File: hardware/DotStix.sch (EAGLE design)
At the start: 15 parts, among them U1 ATMEGA328P-MU-QFN32

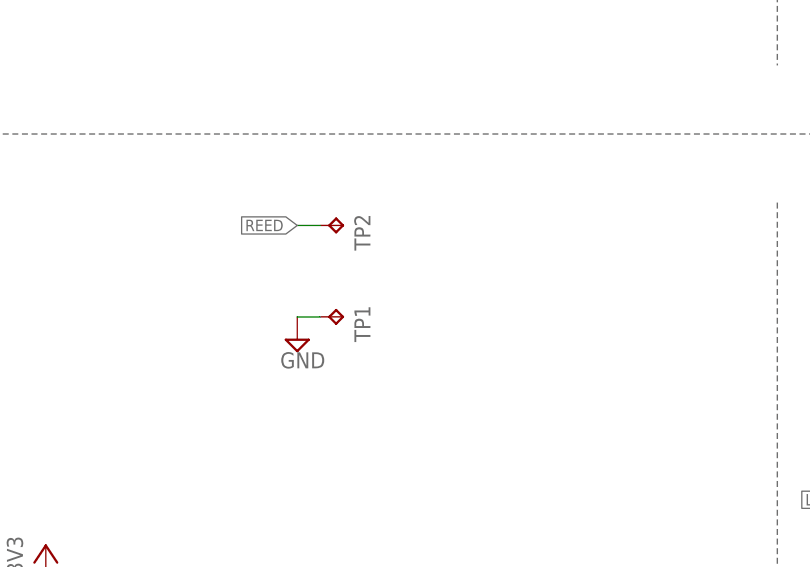
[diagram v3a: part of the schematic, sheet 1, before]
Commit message: Add HexID, second reed on rear side
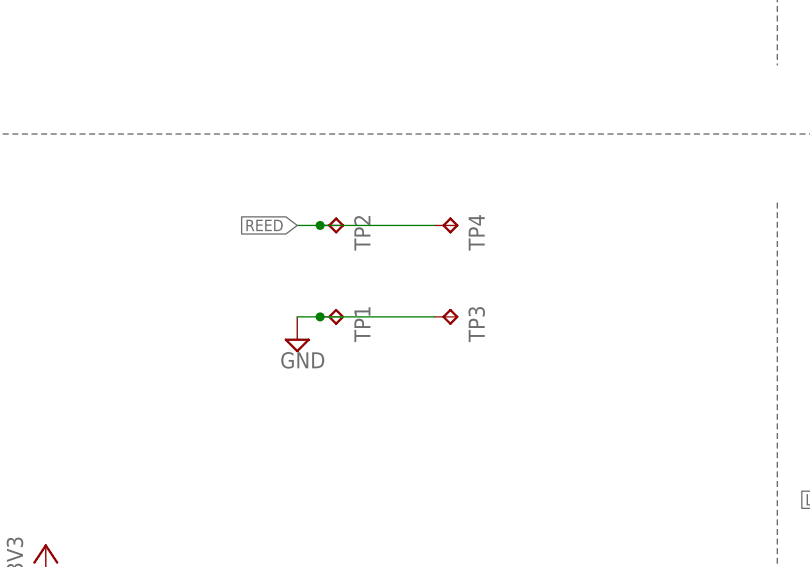
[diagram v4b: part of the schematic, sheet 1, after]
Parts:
- added TP3, TP4: TPTP20SQ, testpad:TPTP20SQ
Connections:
- net GND: now also TP3.TP
- net REED: now also TP4.TP
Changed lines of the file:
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@@
 <part name="+3V9" library="supply1" deviceset="+3V3" device=""/>
 <part name="SUPPLY10" library="supply2" deviceset="GND" device=""/>
+<part name="TP3" library="testpad" deviceset="TP" device="TP20SQ"/>
+<part name="TP4" library="testpad" deviceset="TP" device="TP20SQ"/>
 </parts>
 <sheets>
@@
 <instance part="+3V9" gate="G$1" x="48.26" y="55.88"/>
 <instance part="SUPPLY10" gate="GND" x="-6.35" y="39.37"/>
+<instance part="TP3" gate="G$1" x="93.98" y="81.28" rot="R270"/>
+<instance part="TP4" gate="G$1" x="93.98" y="91.44" rot="R270"/>
 </instances>
 <busses>
@@
 <pinref part="SUPPLY5" gate="GND" pin="GND"/>
 <wire x1="78.74" y1="81.28" x2="76.2" y2="81.28" width="0.1524" layer="91"/>
+<pinref part="TP3" gate="G$1" pin="TP"/>
+<wire x1="91.44" y1="81.28" x2="78.74" y2="81.28" width="0.1524" layer="91"/>
+<junction x="78.74" y="81.28"/>
 </segment>
 <segment>
@@
 <net name="REED" class="0">
 <segment>
+<pinref part="U1" gate="G$1" pin="PB2(SS/OC1B/PCINT2)"/>
+<wire x1="195.58" y1="81.28" x2="198.12" y2="81.28" width="0.1524" layer="91"/>
+<label x="198.12" y="81.28" size="1.27" layer="95" xref="yes"/>
+</segment>
+<segment>
+<pinref part="TP4" gate="G$1" pin="TP"/>
 <pinref part="TP2" gate="G$1" pin="TP"/>
 <wire x1="78.74" y1="91.44" x2="76.2" y2="91.44" width="0.1524" layer="91"/>
 <label x="76.2" y="91.44" size="1.27" layer="95" rot="R180" xref="yes"/>
-</segment>
-<segment>
-<pinref part="U1" gate="G$1" pin="PB2(SS/OC1B/PCINT2)"/>
-<wire x1="195.58" y1="81.28" x2="198.12" y2="81.28" width="0.1524" layer="91"/>
-<label x="198.12" y="81.28" size="1.27" layer="95" xref="yes"/>
-</segment>
-</net>
+<wire x1="91.44" y1="91.44" x2="78.74" y2="91.44" width="0.1524" layer="91"/>
+<junction x="78.74" y="91.44"/>
+</segment>
+</net>

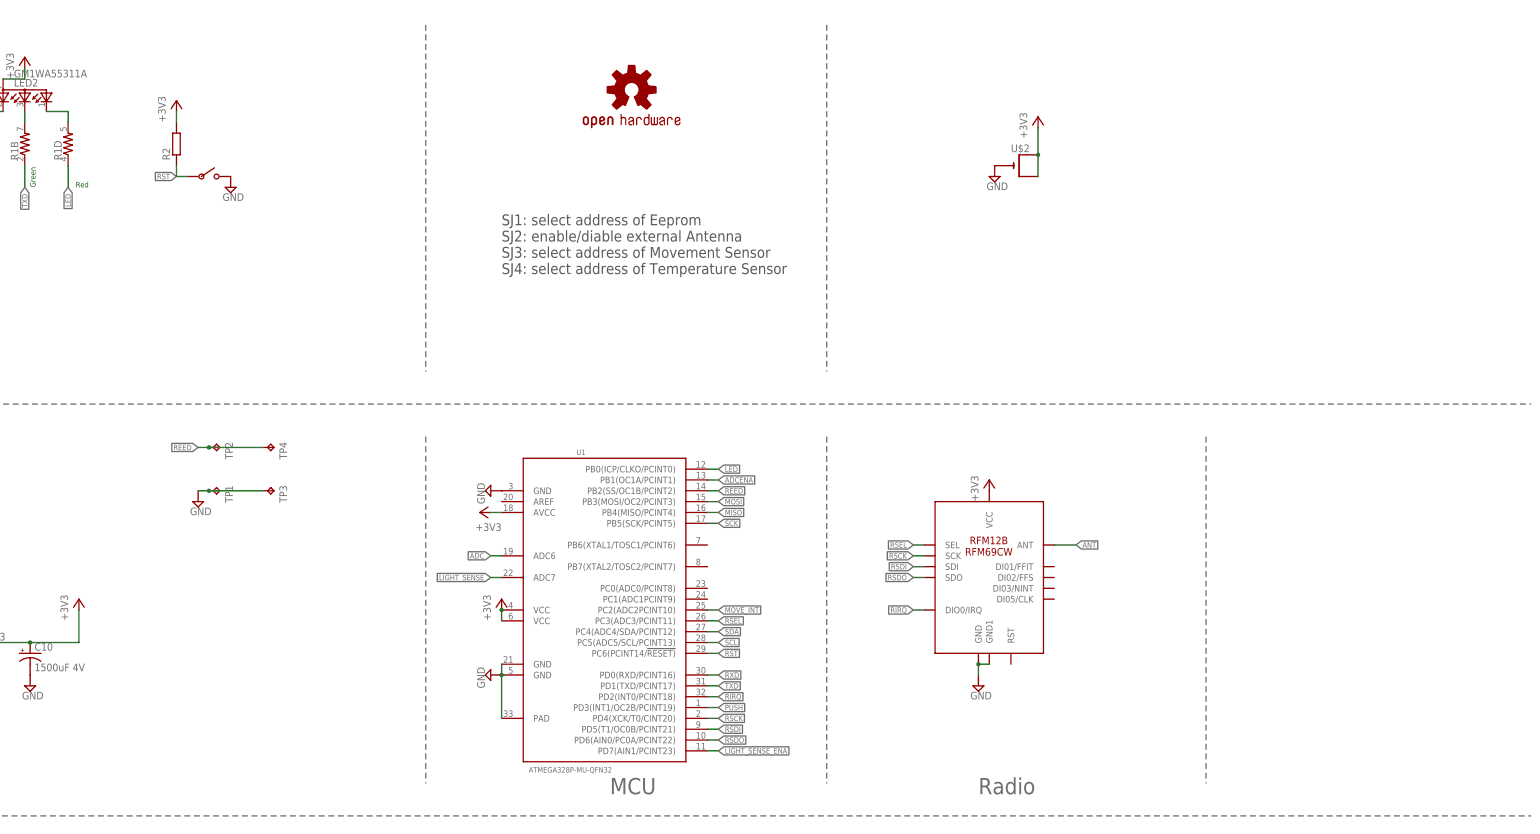
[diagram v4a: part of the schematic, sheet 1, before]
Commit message: Add photoresistor
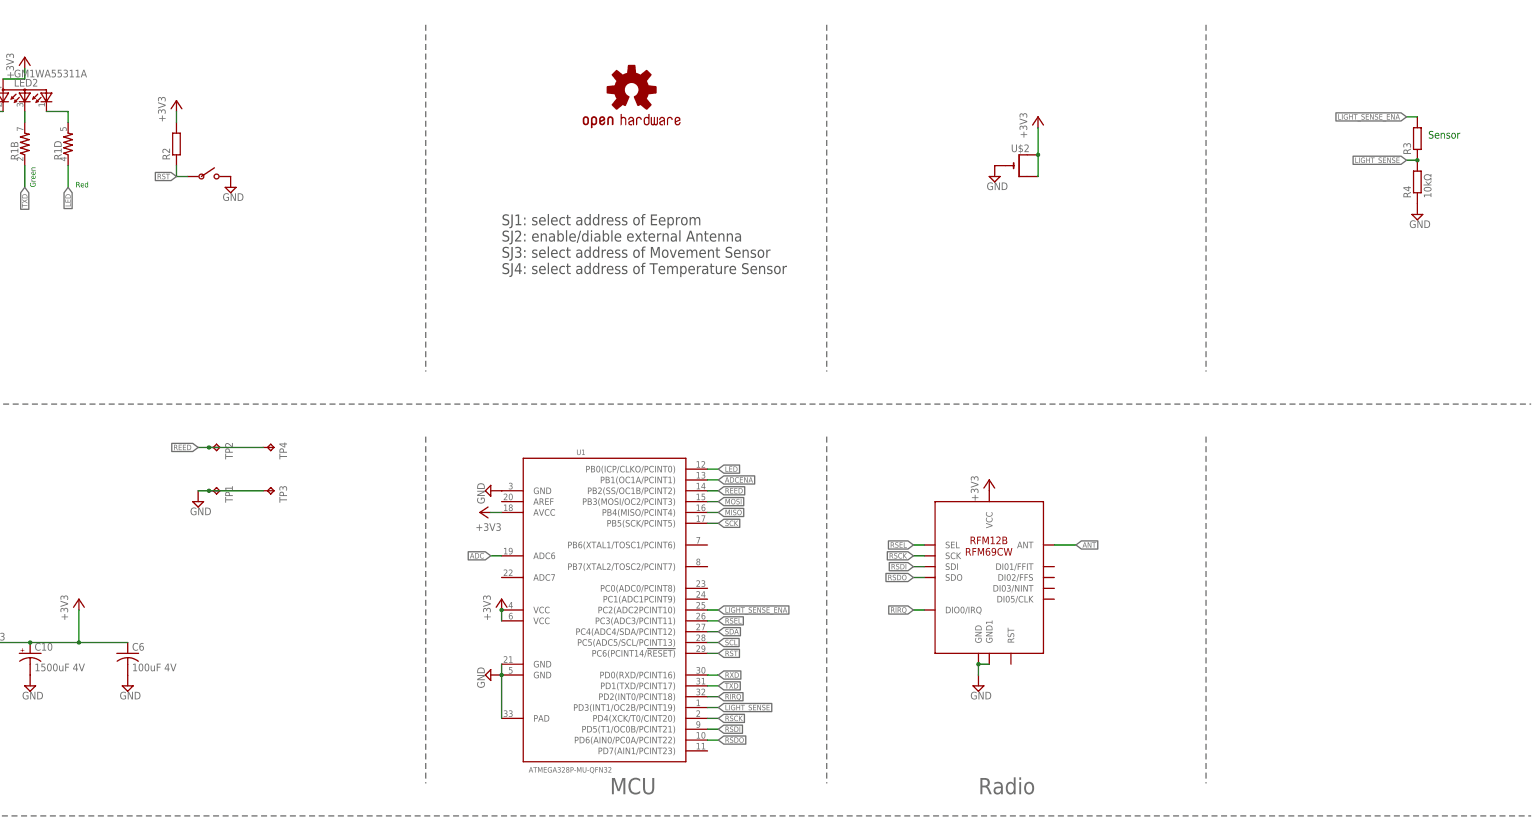
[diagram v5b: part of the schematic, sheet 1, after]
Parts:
- added C6: 100uF 4V, adafruit:C-USC3216
- added R3: (no value), resistor:R-EU_R0805
- added R4: 10kΩ, resistor:R-EU_R0603
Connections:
- removed net MOVE_INT: U1.PC2(ADC2PCINT10)
- removed net PUSH: U1.PD3(INT1/OC2B/PCINT19)
- net +3V3: now also C6.1
- net GND: now also C6.2, R4.1
- net LIGHT_SENSE: now also R3.1, R4.2, U1.PD3(INT1/OC2B/PCINT19); no longer U1.ADC7
- net LIGHT_SENSE_ENA: now also R3.2, U1.PC2(ADC2PCINT10); no longer U1.PD7(AIN1/PCINT23)
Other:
- note added: "Sensor"
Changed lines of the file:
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@@
 <part name="TP3" library="testpad" deviceset="TP" device="TP20SQ"/>
 <part name="TP4" library="testpad" deviceset="TP" device="TP20SQ"/>
+<part name="SUPPLY16" library="supply2" deviceset="GND" device=""/>
+<part name="C6" library="adafruit" deviceset="C-US" device="C3216" value="100uF 4V"/>
+<part name="R3" library="resistor" deviceset="R-EU_" device="R0805"/>
+<part name="R4" library="resistor" deviceset="R-EU_" device="R0603" value="10kΩ"/>
+<part name="SUPPLY14" library="supply2" deviceset="GND" device=""/>
 </parts>
 <sheets>
@@
 <text x="38.1" y="152.4" size="1.27" layer="91" rot="R90">Green</text>
 <text x="47.498" y="152.4" size="1.27" layer="91">Red</text>
+<wire x1="312.42" y1="190.5" x2="312.42" y2="109.22" width="0.1524" layer="95" style="longdash"/>
+<text x="364.49" y="163.83" size="1.778" layer="91">Sensor</text>
 </plain>
 <instances>
@@
 <instance part="TP3" gate="G$1" x="93.98" y="81.28" rot="R270"/>
 <instance part="TP4" gate="G$1" x="93.98" y="91.44" rot="R270"/>
+<instance part="SUPPLY16" gate="GND" x="59.69" y="35.56"/>
+<instance part="C6" gate="G$1" x="59.69" y="43.18"/>
+<instance part="R3" gate="G$1" x="361.95" y="163.83" rot="R90"/>
+<instance part="R4" gate="G$1" x="361.95" y="153.67" rot="R90"/>
+<instance part="SUPPLY14" gate="GND" x="361.95" y="146.05"/>
 </instances>
 <busses>
@@
 <wire x1="-6.35" y1="45.72" x2="-6.35" y2="41.91" width="0.1524" layer="91"/>
 </segment>
+<segment>
+<pinref part="SUPPLY16" gate="GND" pin="GND"/>
+<pinref part="C6" gate="G$1" pin="2"/>
+</segment>
+<segment>
+<pinref part="R4" gate="G$1" pin="1"/>
+<pinref part="SUPPLY14" gate="GND" pin="GND"/>
+</segment>
 </net>
 <net name="SDA" class="0">
@@
 <label x="45.72" y="152.4" size="1.27" layer="95" rot="R270" xref="yes"/>
 <pinref part="R1" gate="D" pin="1"/>
-</segment>
-</net>
-<net name="LIGHT_SENSE" class="0">
-<segment>
-<pinref part="U1" gate="G$1" pin="ADC7"/>
-<wire x1="147.32" y1="60.96" x2="144.78" y2="60.96" width="0.1524" layer="91"/>
-<label x="144.78" y="60.96" size="1.27" layer="95" rot="R180" xref="yes"/>
-</segment>
-</net>
-<net name="LIGHT_SENSE_ENA" class="0">
-<segment>
-<pinref part="U1" gate="G$1" pin="PD7(AIN1/PCINT23)"/>
-<wire x1="195.58" y1="20.32" x2="198.12" y2="20.32" width="0.1524" layer="91"/>
-<label x="198.12" y="20.32" size="1.27" layer="95" xref="yes"/>
 </segment>
 </net>
@@
 <pinref part="+3V9" gate="G$1" pin="+3V3"/>
 <wire x1="48.26" y1="53.34" x2="48.26" y2="45.72" width="0.1524" layer="91"/>
+<pinref part="C6" gate="G$1" pin="1"/>
+<wire x1="48.26" y1="45.72" x2="59.69" y2="45.72" width="0.1524" layer="91"/>
+<junction x="48.26" y="45.72"/>
 </segment>
 </net>
@@
 <wire x1="195.58" y1="45.72" x2="198.12" y2="45.72" width="0.1524" layer="91"/>
 <label x="198.12" y="45.72" size="1.27" layer="95" xref="yes"/>
-</segment>
-</net>
-<net name="PUSH" class="0">
-<segment>
-<pinref part="U1" gate="G$1" pin="PD3(INT1/OC2B/PCINT19)"/>
-<wire x1="195.58" y1="30.48" x2="198.12" y2="30.48" width="0.1524" layer="91"/>
-<label x="198.12" y="30.48" size="1.27" layer="95" xref="yes"/>
-</segment>
-</net>
-<net name="MOVE_INT" class="0">
-<segment>
-<pinref part="U1" gate="G$1" pin="PC2(ADC2PCINT10)"/>
-<wire x1="195.58" y1="53.34" x2="198.12" y2="53.34" width="0.1524" layer="91"/>
-<label x="198.12" y="53.34" size="1.27" layer="95" xref="yes"/>
 </segment>
 </net>
@@
 </segment>
 </net>
+<net name="LIGHT_SENSE" class="0">
+<segment>
+<pinref part="U1" gate="G$1" pin="PD3(INT1/OC2B/PCINT19)"/>
+<wire x1="195.58" y1="30.48" x2="198.12" y2="30.48" width="0.1524" layer="91"/>
+<label x="198.12" y="30.48" size="1.27" layer="95" xref="yes"/>
+</segment>
+<segment>
+<pinref part="R4" gate="G$1" pin="2"/>
+<wire x1="361.95" y1="158.75" x2="359.41" y2="158.75" width="0.1524" layer="91"/>
+<pinref part="R3" gate="G$1" pin="1"/>
+<junction x="361.95" y="158.75"/>
+<label x="359.41" y="158.75" size="1.27" layer="95" rot="R180" xref="yes"/>
+</segment>
+</net>
+<net name="LIGHT_SENSE_ENA" class="0">
+<segment>
+<pinref part="R3" gate="G$1" pin="2"/>
+<wire x1="361.95" y1="168.91" x2="359.41" y2="168.91" width="0.1524" layer="91"/>
+<label x="359.41" y="168.91" size="1.27" layer="95" rot="R180" xref="yes"/>
+</segment>
+<segment>
+<pinref part="U1" gate="G$1" pin="PC2(ADC2PCINT10)"/>
+<wire x1="195.58" y1="53.34" x2="198.12" y2="53.34" width="0.1524" layer="91"/>
+<label x="198.12" y="53.34" size="1.27" layer="95" xref="yes"/>
+</segment>
+</net>

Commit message: Minor info improvements
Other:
- note removed: "0x44 / yes"
- note removed: "0x48 / yes, temperature-dependent values, incorrect (70 degC)"
- note removed: "0x50 & 0x51 (a16 bit) / yes"
- note removed: "0x60 / yes"
- note removed: "0x68 / yes"
- note removed: "0x77 / no ??"
- note removed: "1000100D"
- note removed: "100100XD"
- note removed: "1010XXXD"
- note removed: "1100000D"
- note removed: "110100XD"
- note removed: "1110111D"
- note removed: "9DoF"
- note removed: "BMP18"
- note removed: "CAT24M01"
- note removed: "D = Direction"
- note removed: "EEPROM 1Mbit"
- note removed: "Ext Oscillator - Low Fuse : 0x5F"
- note removed: "Hex Address / Tested?"
- note removed: "I2C Address"
- note removed: "ISL29125"
- note removed: "MPU9250"
- note removed: "Part #"
- note removed: "RGB"
- note removed: "SI1145"
- note removed: "Sensor / Memory"
- note removed: "TMP102 or TMP112 (high acc +/-0.5°)"
- note removed: "TMP102/112"
- note removed: "Temp/Pressure"
- note removed: "Temperature"
- note removed: "UV"
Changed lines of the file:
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@@
 <setting verticaltext="up"/>
 </settings>
-<grid distance="0.05" unitdist="inch" unit="inch" style="lines" multiple="1" display="no" altdistance="0.01" altunitdist="inch" altunit="inch"/>
+<grid distance="0.1" unitdist="inch" unit="inch" style="lines" multiple="1" display="no" altdistance="0.01" altunitdist="inch" altunit="inch"/>
 <layers>
 <layer number="1" name="Top" color="4" fill="1" visible="no" active="no"/>
@@
 <text x="259.08" y="10.16" size="3.81" layer="95">Radio</text>
 <wire x1="312.42" y1="93.98" x2="312.42" y2="12.7" width="0.1524" layer="95" style="longdash"/>
-<text x="175.26" y="0" size="1.016" layer="91" align="center">TMP102 or TMP112 (high acc +/-0.5°)</text>
 <text x="21.59" y="152.4" size="1.27" layer="91">Blue</text>
 <text x="38.1" y="152.4" size="1.27" layer="91" rot="R90">Green</text>
@@
 </nets>
 </sheet>
-<sheet>
-<plain>
-<text x="2.54" y="81.28" size="1.6764" layer="91">Sensor / Memory</text>
-<text x="27.94" y="81.28" size="1.6764" layer="91">Part #</text>
-<text x="48.26" y="81.28" size="1.6764" layer="91">I2C Address</text>
-<text x="5.08" y="73.66" size="1.27" layer="91">RGB</text>
-<text x="27.94" y="73.66" size="1.27" layer="91">ISL29125</text>
-<text x="48.26" y="73.66" size="1.27" layer="91">1000100D</text>
-<text x="5.08" y="68.58" size="1.27" layer="91">UV</text>
-<text x="27.94" y="68.58" size="1.27" layer="91">SI1145</text>
-<text x="48.26" y="68.58" size="1.27" layer="91">1100000D</text>
-<text x="5.08" y="63.5" size="1.27" layer="91">Temperature</text>
-<text x="27.94" y="63.5" size="1.27" layer="91">TMP102/112</text>
-<text x="48.26" y="63.5" size="1.27" layer="91">100100XD</text>
-<text x="5.08" y="58.42" size="1.27" layer="91">9DoF</text>
-<text x="27.94" y="58.42" size="1.27" layer="91">MPU9250</text>
-<text x="48.26" y="58.42" size="1.27" layer="91">110100XD</text>
-<text x="68.58" y="81.28" size="1.778" layer="91">Hex Address / Tested?</text>
-<text x="76.2" y="73.66" size="1.27" layer="91">0x44 / yes</text>
-<text x="76.2" y="68.58" size="1.27" layer="91">0x60 / yes</text>
-<text x="5.08" y="53.34" size="1.27" layer="91">Temp/Pressure</text>
-<text x="27.94" y="53.34" size="1.27" layer="91">BMP18</text>
-<text x="48.26" y="53.34" size="1.27" layer="91">1110111D</text>
-<text x="76.2" y="53.34" size="1.27" layer="91">0x77 / no ??</text>
-<text x="76.2" y="63.5" size="1.27" layer="91">0x48 / yes, temperature-dependent values, incorrect (70 degC)</text>
-<text x="5.08" y="48.26" size="1.27" layer="91">EEPROM 1Mbit</text>
-<text x="27.94" y="48.26" size="1.27" layer="91">CAT24M01 </text>
-<text x="48.26" y="48.26" size="1.27" layer="91">1010XXXD</text>
-<text x="76.2" y="48.26" size="1.27" layer="91">0x50 &amp; 0x51 (a16 bit) / yes</text>
-<text x="48.26" y="78.74" size="1.016" layer="91">D = Direction</text>
-<text x="76.2" y="58.42" size="1.27" layer="91">0x68 / yes</text>
-<text x="5.08" y="27.94" size="1.778" layer="91">Ext Oscillator - Low Fuse : 0x5F</text>
-</plain>
-<instances>
-</instances>
-<busses>
-</busses>
-<nets>
-</nets>
-</sheet>

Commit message: Draft: Fix solar polarity, add 20ppm crystal
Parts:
- removed C10: 1500uF 4V, adafruit:CPOL-USCT7343
- removed C6: 100uF 4V, adafruit:C-USC3216
- added C7, C9: 7pF, rcl:C-EUC0603
- added Y1: (no value), SparkFun-Clocks:RESONATORSMD-3.2X1.3
- added Y2: (no value), SparkFun-Clocks:CRYSTALSMD-3.2X1.5
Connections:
- removed net ADCENA: U1.PB1(OC1A/PCINT1)
- removed net LED: R1D.1, U1.PB0(ICP/CLKO/PCINT0)
- removed net N$12: LED2.CRED, R1C.2
- removed net N$5: LED2.CBLUE, R1B.2
- removed net N$9: LED2.CGREEN, R1D.2
- removed net RXD: R1C.1, U1.PD0(RXD/PCINT16)
- removed net TXD: R1B.1, U1.PD1(TXD/PCINT17)
- new net LED_BLUE: R1B.1, U1.PB1(OC1A/PCINT1)
- new net LED_GREEN: R1A.1, U1.PB2(SS/OC1B/PCINT2)
- new net LED_RED: R1C.1, U1.PB0(ICP/CLKO/PCINT0)
- new net N$1: LED2.CRED, R1B.2
- new net N$3: LED2.CBLUE, R1A.2
- new net N$4: LED2.CGREEN, R1C.2
- new net XTAL1: C9.1, U1.PB6(XTAL1/TOSC1/PCINT6), Y1.3, Y2.2
- new net XTAL2: C7.1, U1.PB7(XTAL2/TOSC2/PCINT7), Y1.1, Y2.1
- net +3V3: no longer C10.+, C6.1
- net GND: now also C7.2, C9.2, D1.C, Y1.2; no longer C10.-, C6.2, D1.A
- net REED: now also U1.PD1(TXD/PCINT17); no longer U1.PB2(SS/OC1B/PCINT2)
- net SOLAR_RAW: now also D1.A; no longer D1.C
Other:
- note removed: "Blue"
- note removed: "Green"
- note removed: "Red"
- moved on the sheet: D1, R1A, R1B, R1C, R1D
